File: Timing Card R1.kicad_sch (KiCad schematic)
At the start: 26 parts, among them J1 71430-0101, J2 Conn_01x10

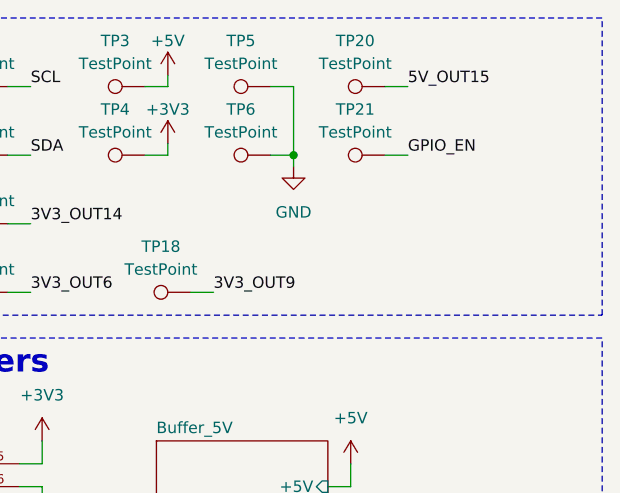
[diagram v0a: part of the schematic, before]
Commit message: Fixed board size
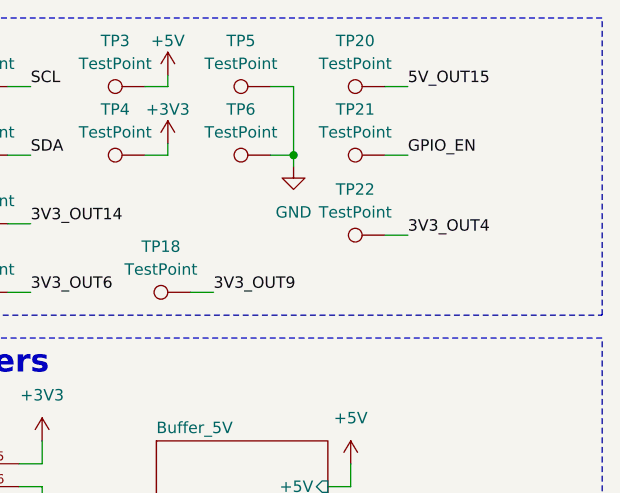
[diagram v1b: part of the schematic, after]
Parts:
- added TP22: TestPoint, TestPoint:TestPoint_Pad_D1.0mm, symbol Connector:TestPoint
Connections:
- net 3V3_OUT4: now also TP22.1
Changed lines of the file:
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@@
 	(wire
 		(pts
+			(xy 259.08 38.1) (xy 261.62 38.1)
+		)
+		(stroke
+			(width 0)
+			(type default)
+		)
+	)
+	(wire
+		(pts
 			(xy 218.44 121.92) (xy 233.68 121.92)
 		)
@@
 		)
 	)
+	(label "3V3_OUT4"
+		(at 261.62 38.1 0)
+		(effects
+			(font
+				(size 1.27 1.27)
+			)
+			(justify left bottom)
+		)
+	)
 	(label "3V3_IN3"
 		(at 124.46 86.36 0)
@@
 					(unit 1)
 				)
+			)
+		)
+	)
+	(symbol
+		(lib_id "Connector:TestPoint")
+		(at 259.08 38.1 90)
+		(unit 1)
+		(exclude_from_sim no)
+		(in_bom yes)
+		(on_board yes)
+		(dnp no)
+		(fields_autoplaced yes)
+		(property "Reference" "TP22"
+			(at 255.778 33.02 90)
+			(effects
+				(font
+					(size 1.27 1.27)
+				)
+			)
+		)
+		(property "Value" "TestPoint"
+			(at 255.778 35.56 90)
+			(effects
+				(font
+					(size 1.27 1.27)
+				)
+			)
+		)
+		(property "Footprint" "TestPoint:TestPoint_Pad_D1.0mm"
+			(at 259.08 33.02 0)
+			(effects
+				(font
+					(size 1.27 1.27)
+				)
+				(hide yes)
+			)
+		)
+		(property "Datasheet" "~"
+			(at 259.08 33.02 0)
+			(effects
+				(font
+					(size 1.27 1.27)
+				)
+				(hide yes)
+			)
+		)
+		(property "Description" "test point"
+			(at 259.08 38.1 0)
+			(effects
+				(font
+					(size 1.27 1.27)
+				)
+				(hide yes)
+			)
+		)
+		(pin "1"
+		)
+		(instances
+			(project "Timing Card R1"
+				(path "/fff8b85b-b334-4e51-bf22-f5c588ac7d6b"
+					(reference "TP22")
+					(unit 1)
+				)
